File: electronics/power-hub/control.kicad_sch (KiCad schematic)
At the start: 5 parts, among them J7 SUPERVISOR

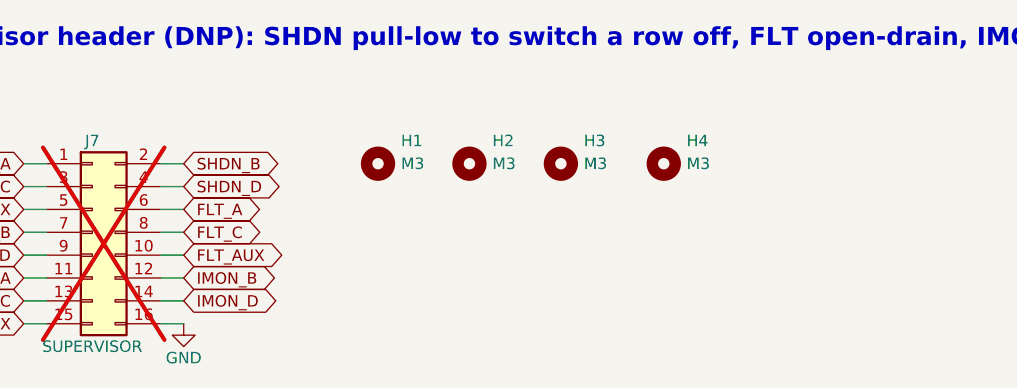
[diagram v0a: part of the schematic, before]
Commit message: Schematics: draw real wires and an overview block diagram
The generator used to connect every pin through a net label only. Now,
in each block, the part with the most pins is the anchor and the
two-pin parts that share a signal with one of its side pins hang off
that pin on a real wire; parts chained behind them (R -> C -> GND)
stack underneath, and anchor-less blocks (pull-ups, reset/boot
buttons) are adopted by the anchor they connect to. Power symbols on
side pins point outward; power-flag references are hidden.

The root sheet becomes a block diagram: the supply rails each sheet
uses across the top, and one lane per pair of sheets listing the
signals they share.

Every wired net still carries one label, so net names, ERC (0) and the
PCB's schematic parity (0) are unchanged; the routed PCBs are untouched.

Co-Authored-By: Claude Opus 5.5 <noreply@anthropic.com>
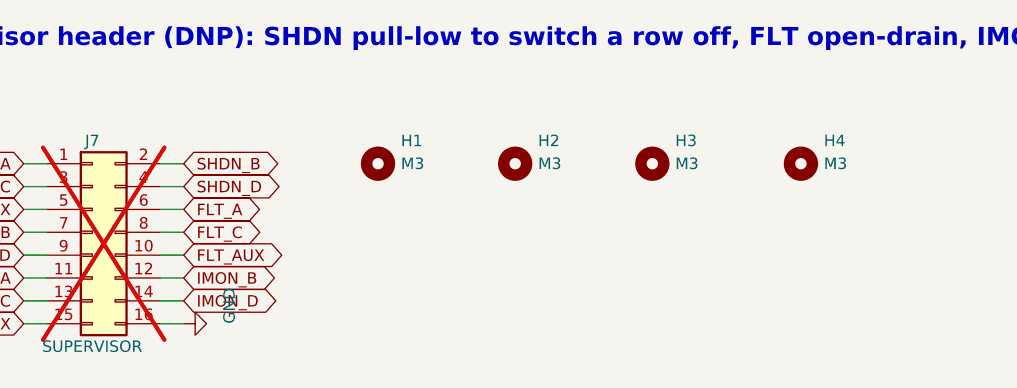
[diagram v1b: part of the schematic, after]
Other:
- moved on the sheet: H2, H3, H4
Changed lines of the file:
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@@
 	(symbol
 		(lib_id "power:GND")
-		(at 52.07 60.96 0)
+		(at 52.07 60.96 90)
 		(unit 1)
 		(exclude_from_sim no)
@@
 		)
 		(property "Value" "GND"
-			(at 52.07 64.77 0)
-			(effects
-				(font
-					(size 1.27 1.27)
-				)
+			(at 57.15 60.96 0)
+			(effects
+				(font
+					(size 1.27 1.27)
+				)
+				(justify left)
 			)
 		)
@@
 	(symbol
 		(lib_id "Mechanical:MountingHole")
-		(at 83.82 43.18 0)
+		(at 88.9 43.18 0)
 		(unit 1)
 		(exclude_from_sim no)
@@
 		(fields_autoplaced yes)
 		(property "Reference" "H2"
-			(at 86.36 40.64 0)
+			(at 91.44 40.64 0)
 			(effects
 				(font
@@
 		)
 		(property "Value" "M3"
-			(at 86.36 43.18 0)
+			(at 91.44 43.18 0)
 			(effects
 				(font
@@
 		)
 		(property "Footprint" "MountingHole:MountingHole_3.2mm_M3"
-			(at 83.82 43.18 0)
-			(effects
-				(font
-					(size 1.27 1.27)
-				)
-				(hide yes)
-			)
-		)
-		(property "Datasheet" ""
-			(at 83.82 43.18 0)
-			(effects
-				(font
-					(size 1.27 1.27)
-				)
-				(hide yes)
-			)
-		)
-		(property "Description" ""
-			(at 83.82 43.18 0)
+			(at 88.9 43.18 0)
+			(effects
+				(font
+					(size 1.27 1.27)
+				)
+				(hide yes)
+			)
+		)
+		(property "Datasheet" ""
+			(at 88.9 43.18 0)
+			(effects
+				(font
+					(size 1.27 1.27)
+				)
+				(hide yes)
+			)
+		)
+		(property "Description" ""
+			(at 88.9 43.18 0)
 			(effects
 				(font
@@
 		)
 		(property "MPN" "M3 mounting hole"
-			(at 83.82 43.18 0)
+			(at 88.9 43.18 0)
 			(effects
 				(font
@@
 		)
 		(property "Manufacturer" "-"
-			(at 83.82 43.18 0)
+			(at 88.9 43.18 0)
 			(effects
 				(font
@@
 	(symbol
 		(lib_id "Mechanical:MountingHole")
-		(at 93.98 43.18 0)
+		(at 104.14 43.18 0)
 		(unit 1)
 		(exclude_from_sim no)
@@
 		(fields_autoplaced yes)
 		(property "Reference" "H3"
-			(at 96.52 40.64 0)
+			(at 106.68 40.64 0)
 			(effects
 				(font
@@
 		)
 		(property "Value" "M3"
-			(at 96.52 43.18 0)
+			(at 106.68 43.18 0)
 			(effects
 				(font
@@
 		)
 		(property "Footprint" "MountingHole:MountingHole_3.2mm_M3"
-			(at 93.98 43.18 0)
-			(effects
-				(font
-					(size 1.27 1.27)
-				)
-				(hide yes)
-			)
-		)
-		(property "Datasheet" ""
-			(at 93.98 43.18 0)
-			(effects
-				(font
-					(size 1.27 1.27)
-				)
-				(hide yes)
-			)
-		)
-		(property "Description" ""
-			(at 93.98 43.18 0)
+			(at 104.14 43.18 0)
+			(effects
+				(font
+					(size 1.27 1.27)
+				)
+				(hide yes)
+			)
+		)
+		(property "Datasheet" ""
+			(at 104.14 43.18 0)
+			(effects
+				(font
+					(size 1.27 1.27)
+				)
+				(hide yes)
+			)
+		)
+		(property "Description" ""
+			(at 104.14 43.18 0)
 			(effects
 				(font
@@
 		)
 		(property "MPN" "M3 mounting hole"
-			(at 93.98 43.18 0)
+			(at 104.14 43.18 0)
 			(effects
 				(font
@@
 		)
 		(property "Manufacturer" "-"
-			(at 93.98 43.18 0)
+			(at 104.14 43.18 0)
 			(effects
 				(font
@@
 	(symbol
 		(lib_id "Mechanical:MountingHole")
-		(at 105.41 43.18 0)
+		(at 120.65 43.18 0)
 		(unit 1)
 		(exclude_from_sim no)
@@
 		(fields_autoplaced yes)
 		(property "Reference" "H4"
-			(at 107.95 40.64 0)
+			(at 123.19 40.64 0)
 			(effects
 				(font
@@
 		)
 		(property "Value" "M3"
-			(at 107.95 43.18 0)
+			(at 123.19 43.18 0)
 			(effects
 				(font
@@
 		)
 		(property "Footprint" "MountingHole:MountingHole_3.2mm_M3"
-			(at 105.41 43.18 0)
-			(effects
-				(font
-					(size 1.27 1.27)
-				)
-				(hide yes)
-			)
-		)
-		(property "Datasheet" ""
-			(at 105.41 43.18 0)
-			(effects
-				(font
-					(size 1.27 1.27)
-				)
-				(hide yes)
-			)
-		)
-		(property "Description" ""
-			(at 105.41 43.18 0)
+			(at 120.65 43.18 0)
+			(effects
+				(font
+					(size 1.27 1.27)
+				)
+				(hide yes)
+			)
+		)
+		(property "Datasheet" ""
+			(at 120.65 43.18 0)
+			(effects
+				(font
+					(size 1.27 1.27)
+				)
+				(hide yes)
+			)
+		)
+		(property "Description" ""
+			(at 120.65 43.18 0)
 			(effects
 				(font
@@
 		)
 		(property "MPN" "M3 mounting hole"
-			(at 105.41 43.18 0)
+			(at 120.65 43.18 0)
 			(effects
 				(font
@@
 		)
 		(property "Manufacturer" "-"
-			(at 105.41 43.18 0)
-			(effects
-				(font
+			(at 120.65 43.18 0)
+			(effects
+				(font

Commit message: Boards v0.2: LMR51635 buck, JST PH, drawn schematics, thermal reliefs
Addresses Fabio's review of v0.1.

Bay node (rev 0.2):
- 5 V buck: LMR51635YDDCR (60 V, 3.5 A, synchronous, 1.1 MHz) with a
  3.3 uH FXL0630, 3 x 22 uF out, 2 x 10 uF + 100 nF in, FB 120k/22k
  (5.16 V), EN 1M/100k UVLO (13.5 V on, 10.8 V off). Replaces the
  TPS54360B, its Schottky and compensation network. CIN straddles the
  VIN/GND pins on solid top-side islands with vias to In1 (TI SLUSF64B).
- 24 V in/out on JST PH (carrier notches resized, rack.yaml pwr_y).
- Power nets named along the path: 24V_BUS -> +24V -> +5V -> DUT_5V_SW
  -> shunt -> DUT_5V; the INA226 visibly runs from +3V3.
- Stackup S+GND / GND / PWR / S+GND: In2 carries +5V, +3V3 under the
  ESP32 and a protected 24 V bus strip. Outer GND pours kept (without
  them Freerouting left ~25 connections unrouted).

Power hub (rev 0.2): JST VH input instead of the screw terminal, JST PH
row outputs, eFuse limit 1.6 A (RILIM 7.5k) to protect the 2 A contacts.

Generator:
- eda.py: drawn schematic mode (sch= placement, Sheet.wire/tag/frame,
  rotated/mirrored symbols, automatic junctions, per-island labels and
  checks that no wire touches another net); all seven sheets redrawn.
- pcbgen.py: thermal reliefs on every pour (+ <board>.kicad_dru for
  single spokes on fine pitch), configurable inner layers, per-zone
  deferral, fixed vias, DRC-driven fix-up for isolated GND pads.
- JLC CPL fix for the LMR51635 (270 deg); BOM, cables, viewer, docs.

ERC 0, DRC 0 copper errors, 0 unconnected, schematic parity 0 on both.

Co-Authored-By: Claude Opus 5.5 <noreply@anthropic.com>
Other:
- note added: "Mounting (M3)"
- note added: "Supervisor header (DNP): SHDN pulls a row off, FLT open-drain, IMON analog"
- note removed: "Supervisor header (DNP): SHDN pull-low to switch a row off, FLT open-drain, IMON analog"
- moved on the sheet: H1, H2, H3, H4, J7
